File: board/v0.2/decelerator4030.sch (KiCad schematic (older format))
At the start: 81 parts, among them CON1 A3000/A4000_LOCAL_BUS_SLOT, J3 XILINX_JTAG, J4 CONN_2, J5 CONN_4, U1 MC68030FE, U10 74LXC245, U11 74LXC245, U12 MCP9801, U13 DS1086L, U14 XTAL_OSC_DIP8, U15 MCP1826S, U16 IS66WVE4M16, U17 IS66WVE4M16, U18 MC68030RC_PGA, U19 XC9536XL-5VQG44C, U2 XC95144XL-10TQG144C, U20 MCP9801, U3 AS6C3216, U4 AS6C3216, U5 S29AL016J, U6 S29AL016J, U7 PCA9564, U8 74LXC245, U9 74LXC245

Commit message: Removing errors in board
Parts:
- added D4: 1N4148, ~, symbol DIODE
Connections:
- net _BERR: now also D4.2 (A)
- net _CIIN: now also U2.26 (IO1-12)
- net _FPUCS: now reaches CON1.134 (_FPUCS)
- net _FPUCS: now also D4.1 (K)
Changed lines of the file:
@@
 LIBS:valves
 LIBS:xilinx-cplds
-LIBS:amiga
 LIBS:xtal-generic
 LIBS:alliance
@@
 LIBS:digilent
 LIBS:maxim
+LIBS:68k
+LIBS:amiga
+LIBS:issi
 LIBS:decelerator4030-cache
 EELAYER 27 0
@@
 Sheet 1 1
 Title "Decelerator4030"
-Date "26 aug 2015"
+Date "14 dec 2015"
 Rev "0.2"
 Comp ""
@@
 Connection ~ 22300 6100
 Connection ~ 22600 6100
+Text GLabel 10800 4750 3    39   Output ~ 0
+_FPUCS
+Wire Wire Line
+	10800 4750 10800 4150
+Text GLabel 12450 6100 0    39   Input ~ 0
+_FPUCS
+Text GLabel 13650 6100 2    60   BiDi ~ 0
+_BERR
+$Comp
+L DIODE D4
+U 1 1 5664D580
+P 13050 6100
+F 0 "D4" H 13050 6200 40  0000 C CNN
+F 1 "1N4148" H 13050 6000 40  0000 C CNN
+F 2 "~" H 13050 6100 60  0000 C CNN
+F 3 "~" H 13050 6100 60  0000 C CNN
+	1    13050 6100
+	-1   0    0    1
+$EndComp
+Wire Wire Line
+	12450 6100 12850 6100
+Wire Wire Line
+	13250 6100 13650 6100
+Text GLabel 6300 6250 1    39   Input ~ 0
+_CIIN
+Wire Wire Line
+	6300 6250 6300 6550
 $EndSCHEMATC

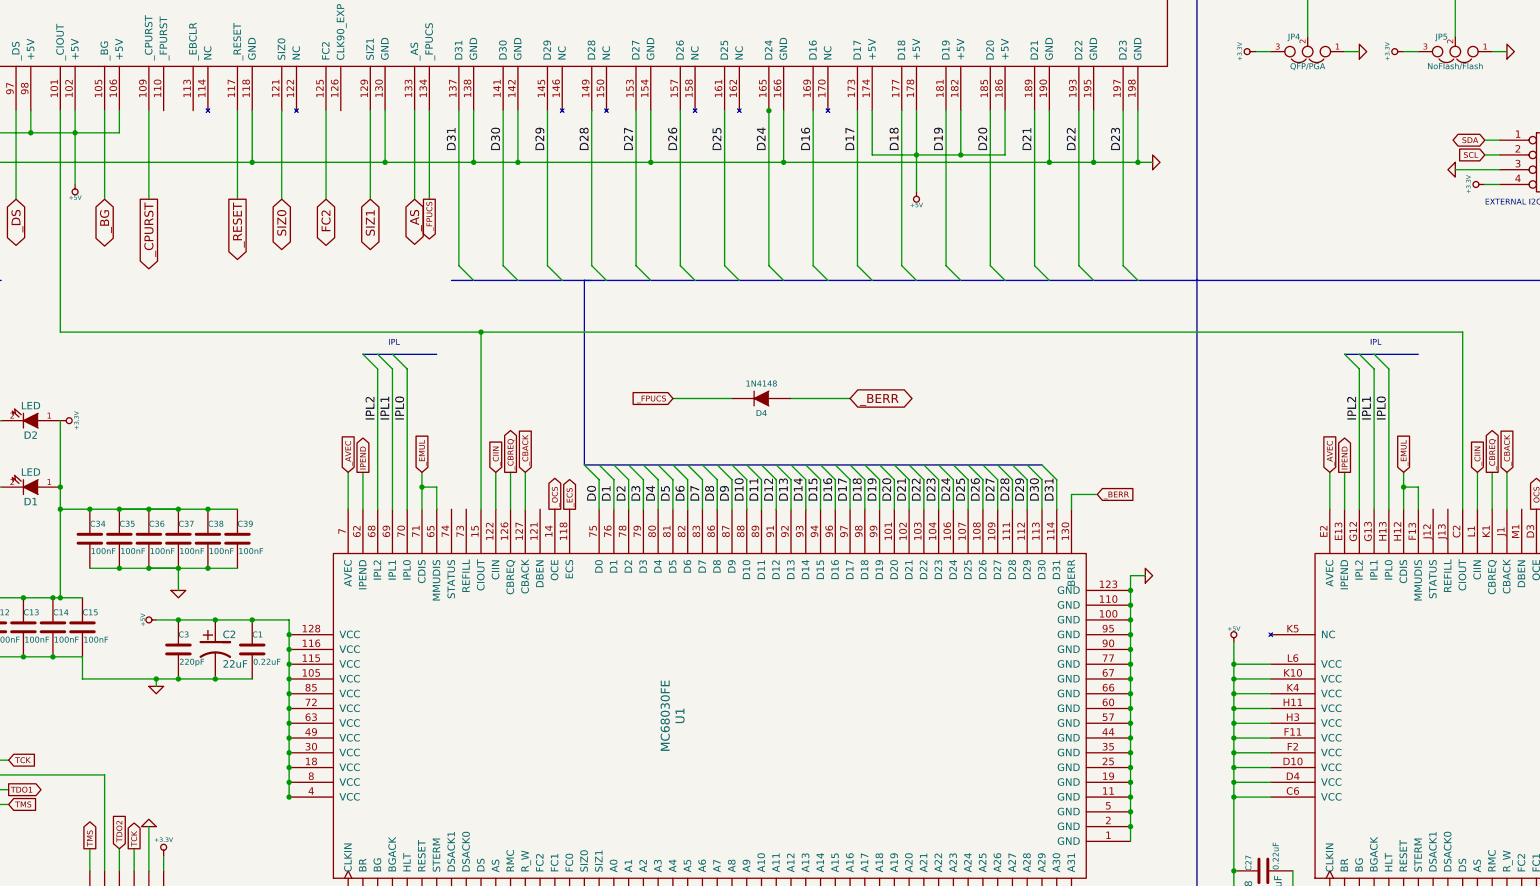
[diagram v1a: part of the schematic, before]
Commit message: Add pull up resistors and _CIIN to CPLD
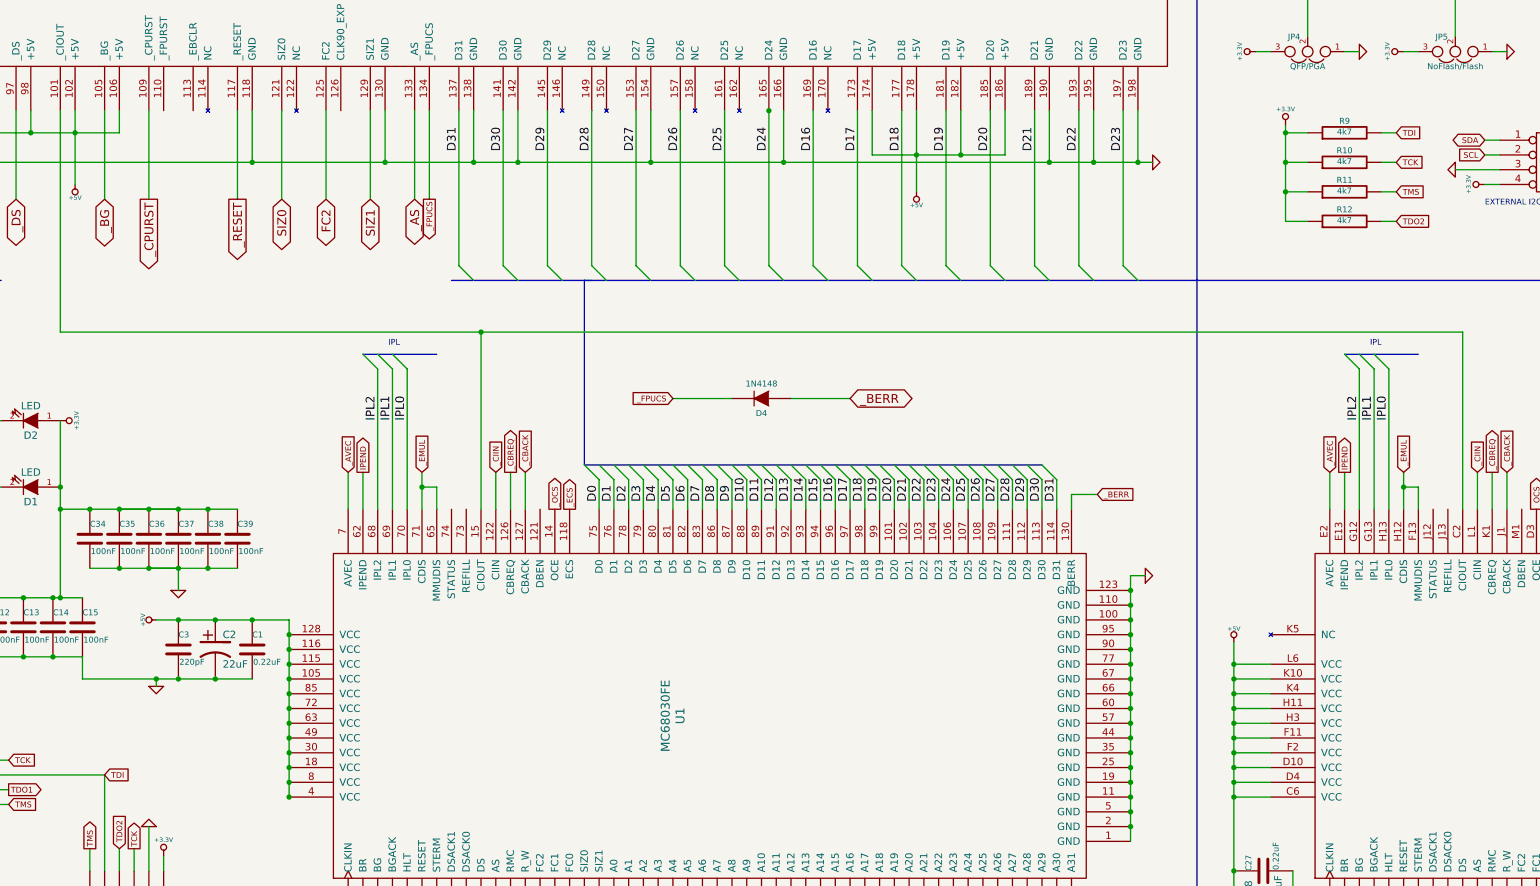
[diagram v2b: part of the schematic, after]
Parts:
- added R10, R11, R12, R9: 4k7, ~, symbol R
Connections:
- net +3.3V: now also R10.1, R11.1, R12.1, R9.1
- net TCK: now also R10.2
- net TDO2: now also R12.2
- net TMS: now also R11.2
- net TDI: now reaches J3.2 (TDI), U2.63 (TDI)
- net TDI: now also R9.2
